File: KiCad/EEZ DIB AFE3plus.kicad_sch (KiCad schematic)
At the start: 11 parts

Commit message: BOM optimization for LCSC
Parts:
- LOGO1: value CR logo -> CE logo
- LOGO2: value Open HW logo -> Open hardware logo
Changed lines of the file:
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@@
 		(in_bom no)
 		(on_board yes)
-		(in_pos_files yes)
+		(in_pos_files no)
 		(dnp no)
 		(property "Reference" "FM2"
-			(at 109.22 190.5 0)
+			(at 110.744 186.944 0)
 			(hide yes)
 			(show_name no)
@@
 		(in_bom no)
 		(on_board yes)
-		(in_pos_files yes)
+		(in_pos_files no)
 		(dnp no)
 		(property "Reference" "FM1"
-			(at 101.6 190.5 0)
+			(at 103.124 186.944 0)
 			(hide yes)
 			(show_name no)
@@
 		(in_bom no)
 		(on_board yes)
-		(in_pos_files yes)
+		(in_pos_files no)
 		(dnp no)
 		(fields_autoplaced yes)
@@
 		(in_bom no)
 		(on_board yes)
-		(in_pos_files yes)
+		(in_pos_files no)
 		(dnp no)
 		(fields_autoplaced yes)
@@
 		(in_bom no)
 		(on_board yes)
-		(in_pos_files yes)
+		(in_pos_files no)
 		(dnp no)
 		(property "Reference" "FM3"
-			(at 116.84 190.5 0)
+			(at 118.364 186.944 0)
 			(hide yes)
 			(show_name no)
@@
 		(in_bom no)
 		(on_board yes)
-		(in_pos_files yes)
+		(in_pos_files no)
 		(dnp no)
 		(fields_autoplaced yes)
@@
 		(in_bom no)
 		(on_board yes)
-		(in_pos_files yes)
+		(in_pos_files no)
 		(dnp no)
 		(fields_autoplaced yes)
@@
 			)
 		)
-		(property "Value" "CR logo"
+		(property "Value" "CE logo"
 			(at 20.32 192.8532 0)
 			(hide yes)
@@
 				(font
 					(size 1.27 1.27)
+				)
+			)
+		)
+		(property "LCSC" ""
+			(at 20.32 190.5 0)
+			(hide yes)
+			(show_name no)
+			(do_not_autoplace no)
+			(effects
+				(font
+					(size 0.889 0.889)
 				)
 			)
@@
 		(in_bom no)
 		(on_board yes)
-		(in_pos_files yes)
+		(in_pos_files no)
 		(dnp no)
 		(fields_autoplaced yes)
@@
 		(in_bom no)
 		(on_board yes)
-		(in_pos_files yes)
+		(in_pos_files no)
 		(dnp no)
 		(property "Reference" "FM4"
-			(at 124.46 190.5 0)
+			(at 125.984 186.944 0)
 			(hide yes)
 			(show_name no)
@@
 		(in_bom no)
 		(on_board yes)
-		(in_pos_files yes)
+		(in_pos_files no)
 		(dnp no)
 		(fields_autoplaced yes)
@@
 			)
 		)
-		(property "Value" "Open HW logo"
+		(property "Value" "Open hardware logo"
 			(at 30.48 192.8416 0)
 			(hide yes)
@@
 				)
 			)
+		)
+		(property "DigiKey" ""
+			(at 30.48 190.5 0)
+			(hide yes)
+			(show_name no)
+			(do_not_autoplace no)
+			(effects
+				(font
+					(size 0.889 0.889)
+				)
+			)
+		)
+		(property "Mouser" ""
+			(at 30.48 190.5 0)
+			(hide yes)
+			(show_name no)
+			(do_not_autoplace no)
+			(effects
+				(font
+					(size 0.889 0.889)
+				)
+			)
+		)
+		(property "TME" ""
+			(at 30.48 190.5 0)
+			(hide yes)
+			(show_name no)
+			(do_not_autoplace no)
+			(effects
+				(font
+					(size 0.889 0.889)
+				)
+			)
+		)
+		(property "LCSC" ""
+			(at 30.48 190.5 0)
+			(hide yes)
+			(show_name no)
+			(do_not_autoplace no)
+			(effects
+				(font
+					(size 0.889 0.889)
+				)
+			)

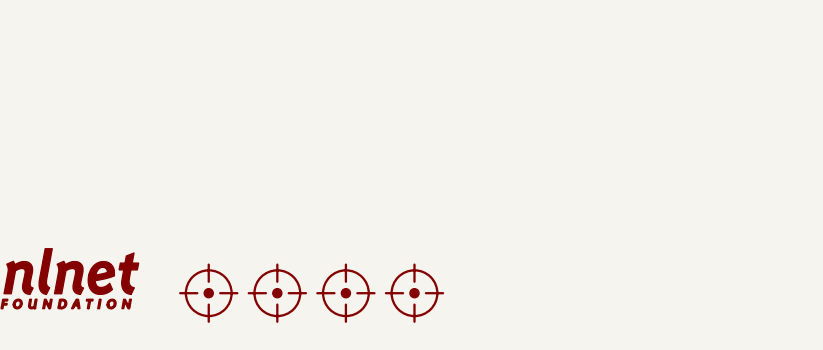
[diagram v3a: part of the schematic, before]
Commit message: OSHWA ID added
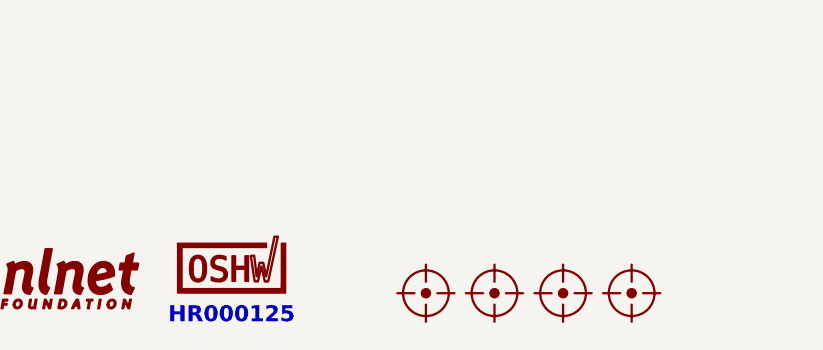
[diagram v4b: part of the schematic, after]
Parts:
- added LOGO8: OSHWA logo, PCM_EEZ_unsorted:OSHWA logo 6.6mm, symbol PCM_EEZ_symbols:OSHWA logo
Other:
- note added: "HR000125"
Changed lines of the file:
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@@
 	(title_block
 		(title "${project_name}")
-		(date "2026-07-20")
+		(date "2026-08-07")
 		(rev "${project_version}")
 		(company "${project_creator}")
@@
 		(comment 2 "${project_info}")
 		(comment 3 "${project_url}")
+	)
+	(text "HR000125"
+		(exclude_from_sim no)
+		(at 104.14 193.04 0)
+		(effects
+			(font
+				(face "DejaVu Sans Mono")
+				(size 1.778 1.778)
+				(bold yes)
+				(color 132 0 0 1)
+			)
+		)
 	)
 	(table
@@
 	(symbol
 		(lib_id "PCM_EEZ_symbols:FIDUCIAL")
-		(at 109.22 190.5 0)
+		(at 133.35 190.5 0)
 		(unit 1)
 		(body_style 1)
@@
 		(dnp no)
 		(property "Reference" "FM2"
-			(at 110.744 186.944 0)
+			(at 134.874 186.944 0)
 			(hide yes)
 			(show_name no)
@@
 		)
 		(property "Value" "FIDUCIAL_2"
-			(at 109.22 190.5 0)
+			(at 133.35 190.5 0)
 			(hide yes)
 			(show_name no)
@@
 		)
 		(property "Footprint" "PCM_EEZ_SMD:Fiducial_0.75mm_Mask1.5mm"
-			(at 109.22 195.58 0)
+			(at 133.35 195.58 0)
 			(hide yes)
 			(show_name no)
@@
 		)
 		(property "Datasheet" ""
-			(at 109.22 190.5 0)
+			(at 133.35 190.5 0)
 			(hide yes)
 			(show_name no)
@@
 		)
 		(property "Description" ""
-			(at 109.22 190.5 0)
+			(at 133.35 190.5 0)
 			(hide yes)
 			(show_name no)
@@
 		)
 		(property "Comment" ""
-			(at 109.22 190.5 0)
+			(at 133.35 190.5 0)
 			(hide yes)
 			(show_name no)
@@
 	(symbol
 		(lib_id "PCM_EEZ_symbols:FIDUCIAL")
-		(at 101.6 190.5 0)
+		(at 125.73 190.5 0)
 		(unit 1)
 		(body_style 1)
@@
 		(dnp no)
 		(property "Reference" "FM1"
-			(at 103.124 186.944 0)
+			(at 127.254 186.944 0)
 			(hide yes)
 			(show_name no)
@@
 		)
 		(property "Value" "FIDUCIAL_2"
-			(at 101.6 190.5 0)
+			(at 125.73 190.5 0)
 			(hide yes)
 			(show_name no)
@@
 		)
 		(property "Footprint" "PCM_EEZ_SMD:Fiducial_0.75mm_Mask1.5mm"
-			(at 101.6 195.58 0)
+			(at 125.73 195.58 0)
 			(hide yes)
 			(show_name no)
@@
 		)
 		(property "Datasheet" ""
-			(at 101.6 190.5 0)
+			(at 125.73 190.5 0)
 			(hide yes)
 			(show_name no)
@@
 		)
 		(property "Description" ""
-			(at 101.6 190.5 0)
+			(at 125.73 190.5 0)
 			(hide yes)
 			(show_name no)
@@
 		)
 		(property "Comment" ""
-			(at 101.6 190.5 0)
+			(at 125.73 190.5 0)
 			(hide yes)
 			(show_name no)
@@
 	(symbol
 		(lib_id "PCM_EEZ_symbols:FIDUCIAL")
-		(at 116.84 190.5 0)
+		(at 140.97 190.5 0)
 		(unit 1)
 		(body_style 1)
@@
 		(dnp no)
 		(property "Reference" "FM3"
-			(at 118.364 186.944 0)
+			(at 142.494 186.944 0)
 			(hide yes)
 			(show_name no)
@@
 		)
 		(property "Value" "FIDUCIAL_2"
-			(at 116.84 190.5 0)
+			(at 140.97 190.5 0)
 			(hide yes)
 			(show_name no)
@@
 		)
 		(property "Footprint" "PCM_EEZ_SMD:Fiducial_0.75mm_Mask1.5mm"
-			(at 116.84 195.58 0)
+			(at 140.97 195.58 0)
 			(hide yes)
 			(show_name no)
@@
 		)
 		(property "Datasheet" ""
-			(at 116.84 190.5 0)
+			(at 140.97 190.5 0)
 			(hide yes)
 			(show_name no)
@@
 		)
 		(property "Description" ""
-			(at 116.84 190.5 0)
+			(at 140.97 190.5 0)
 			(hide yes)
 			(show_name no)
@@
 		)
 		(property "Comment" ""
-			(at 116.84 190.5 0)
+			(at 140.97 190.5 0)
 			(hide yes)
 			(show_name no)
@@
 	)
 	(symbol
+		(lib_id "PCM_EEZ_symbols:OSHWA logo")
+		(at 104.14 187.325 0)
+		(unit 1)
+		(body_style 1)
+		(exclude_from_sim no)
+		(in_bom no)
+		(on_board yes)
+		(in_pos_files yes)
+		(dnp no)
+		(fields_autoplaced yes)
+		(property "Reference" "LOGO8"
+			(at 104.14 184.7975 0)
+			(hide yes)
+			(show_name no)
+			(do_not_autoplace no)
+			(effects
+				(font
+					(size 1.27 1.27)
+				)
+			)
+		)
+		(property "Value" "OSHWA logo"
+			(at 104.14 189.8525 0)
+			(hide yes)
+			(show_name no)
+			(do_not_autoplace no)
+			(effects
+				(font
+					(size 1.27 1.27)
+				)
+			)
+		)
+		(property "Footprint" "PCM_EEZ_unsorted:OSHWA logo 6.6mm"
+			(at 104.14 187.325 0)
+			(hide yes)
+			(show_name no)
+			(do_not_autoplace no)
+			(effects
+				(font
+					(size 1.27 1.27)
+				)
+			)
+		)
+		(property "Datasheet" ""
+			(at 104.14 187.325 0)
+			(hide yes)
+			(show_name no)
+			(do_not_autoplace no)
+			(effects
+				(font
+					(size 1.27 1.27)
+				)
+			)
+		)
+		(property "Description" ""
+			(at 104.14 187.325 0)
+			(hide yes)
+			(show_name no)
+			(do_not_autoplace no)
+			(effects
+				(font
+					(size 1.27 1.27)
+				)
+			)
+		)
+		(instances
+			(project "EEZ DIB AFE3plus"
+				(path "/324c4880-14dd-4339-a8ef-63d64f49eee3"
+					(reference "LOGO8")
+					(unit 1)
+					(variant
+						(name "Ethernet PHY no xtal")
+					)
+				)
+			)
+		)
+	)
+	(symbol
 		(lib_id "PCM_EEZ_symbols:CE logo")
 		(at 20.32 190.5 0)
@@
 	(symbol
 		(lib_id "PCM_EEZ_symbols:FIDUCIAL")
-		(at 124.46 190.5 0)
+		(at 148.59 190.5 0)
 		(unit 1)
 		(body_style 1)
@@
 		(dnp no)
 		(property "Reference" "FM4"
-			(at 125.984 186.944 0)
+			(at 150.114 186.944 0)
 			(hide yes)
 			(show_name no)
@@
 		)
 		(property "Value" "FIDUCIAL_2"
-			(at 124.46 190.5 0)
+			(at 148.59 190.5 0)
 			(hide yes)
 			(show_name no)
@@
 		)
 		(property "Footprint" "PCM_EEZ_SMD:Fiducial_0.75mm_Mask1.5mm"
-			(at 124.46 195.58 0)
+			(at 148.59 195.58 0)
 			(hide yes)
 			(show_name no)
@@
 		)
 		(property "Datasheet" ""
-			(at 124.46 190.5 0)
+			(at 148.59 190.5 0)
 			(hide yes)
 			(show_name no)
@@
 		)
 		(property "Description" ""
-			(at 124.46 190.5 0)
+			(at 148.59 190.5 0)
 			(hide yes)
 			(show_name no)
@@
 		)
 		(property "Comment" ""
-			(at 124.46 190.5 0)
+			(at 148.59 190.5 0)
 			(hide yes)
 			(show_name no)
@@
 		)
 	)
+	(group ""
+		(members "2bec122e-965e-42b5-ac08-7a983977e4ab" "90525c93-826e-4c39-b357-4e48b7aad0c5")
+	)
 	(sheet

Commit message: BOM update, sheets renamed
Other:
- sheet AFE Ch#3 (hi-voltage): file AFE_Ch#3_(hi-voltage).kicad_sch -> AFE_Ch3_(hi-voltage).kicad_sch
- sheet AFE Ch#4 (Hi-current): file AFE_Ch#4_(Hi-current).kicad_sch -> AFE_Ch4_(Hi-current).kicad_sch
- sheet Isolated Ch#1, Ch#2: file Isolated_Ch#1,_Ch#2.kicad_sch -> Isolated_Ch1_Ch2.kicad_sch
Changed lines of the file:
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@@
 	(title_block
 		(title "${project_name}")
-		(date "2026-08-23")
+		(date "2026-09-02")
 		(rev "${project_version}")
 		(company "${project_creator}")
@@
 					(reference "LOGO8")
 					(unit 1)
-					(variant
-						(name "Ethernet PHY no xtal")
-					)
 				)
 			)
@@
 			)
 		)
-		(property "Sheetfile" "AFE_Ch#4_(Hi-current).kicad_sch"
+		(property "Sheetfile" "AFE_Ch4_(Hi-current).kicad_sch"
 			(at 172.72 29.7946 0)
 			(show_name no)
@@
 			)
 		)
-		(property "Sheetfile" "AFE_Ch#3_(hi-voltage).kicad_sch"
+		(property "Sheetfile" "AFE_Ch3_(hi-voltage).kicad_sch"
 			(at 121.92 29.7946 0)
 			(show_name no)
@@
 			)
 		)
-		(property "Sheetfile" "Isolated_Ch#1,_Ch#2.kicad_sch"
+		(property "Sheetfile" "Isolated_Ch1_Ch2.kicad_sch"
 			(at 76.2 29.7946 0)
 			(show_name no)
